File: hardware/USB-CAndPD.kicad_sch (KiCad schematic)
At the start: 28 parts, among them J201 USB_C_Receptacle_USB2.0_16P, J202 USB_C_Receptacle_USB2.0_16P, U201 TPS25730D, U202 TPD2E2U06DCK

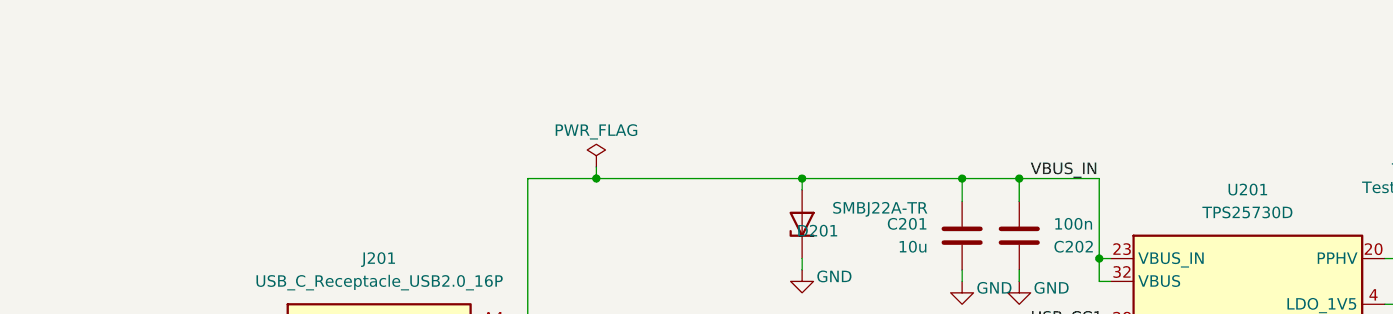
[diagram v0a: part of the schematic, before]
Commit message: Optimized BOM and added netties
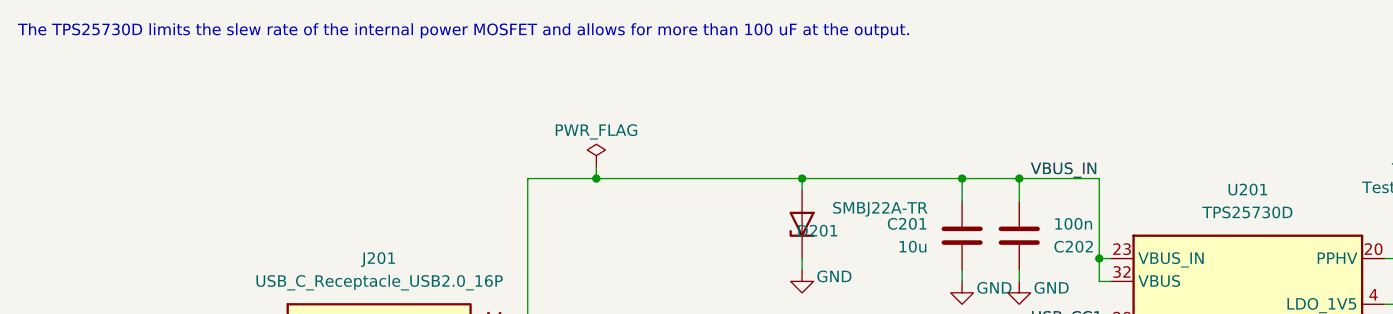
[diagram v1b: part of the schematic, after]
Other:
- note added: "The TPS25730D limits the slew rate of the internal power MOSFET and allows for more than 100 uF at the output."
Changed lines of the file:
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@@
+		)
+	)
+	(text "The TPS25730D limits the slew rate of the internal power MOSFET and allows for more than 100 uF at the output."
+		(exclude_from_sim no)
+		(at 15.748 16.002 0)
+		(effects
+			(font
+				(size 1.27 1.27)
+			)
+			(justify left top)
 		)
 	)

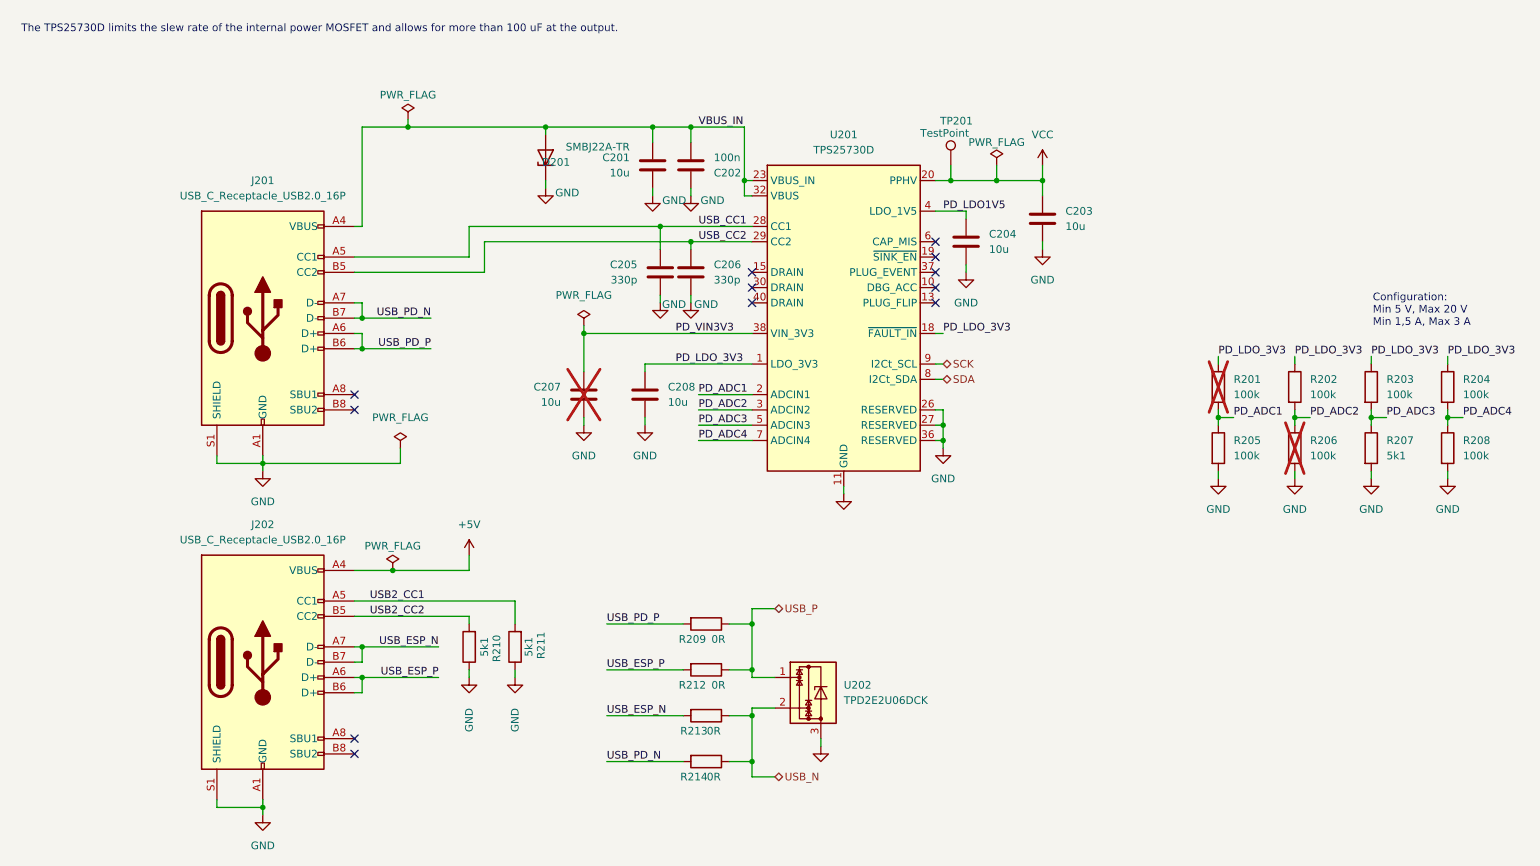
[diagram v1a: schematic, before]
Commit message: Spring terminal, finalising PD settings, checking buck 10 A
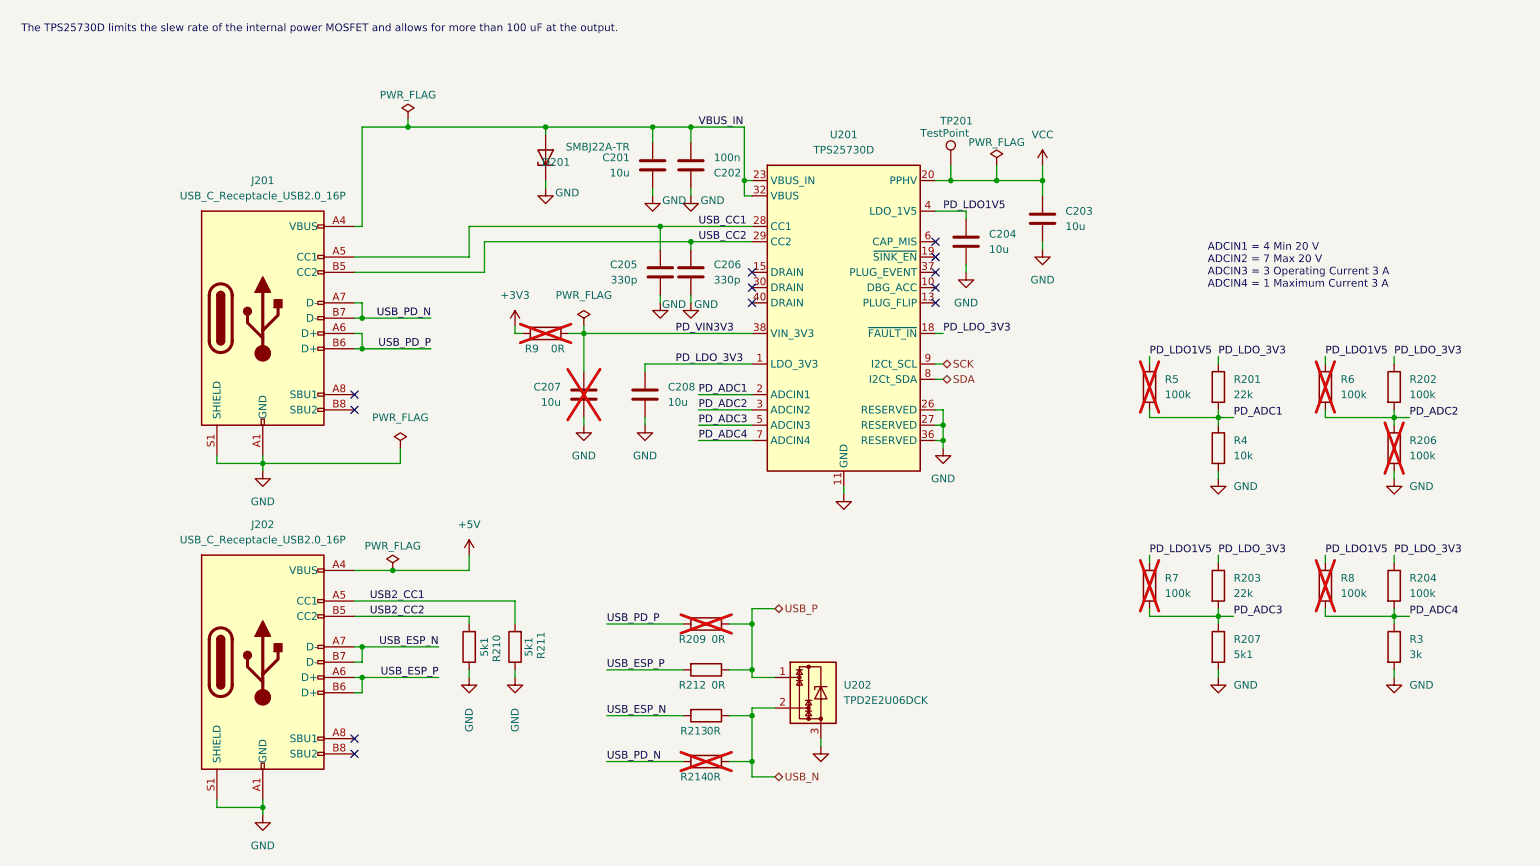
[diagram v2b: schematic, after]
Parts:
- removed R205, R208: 100k, Resistor_SMD:R_0603_1608Metric_Pad0.98x0.95mm_HandSolder, symbol Device:R
- added R3: 3k, Resistor_SMD:R_0603_1608Metric_Pad0.98x0.95mm_HandSolder, symbol Device:R
- added R4: 10k, Resistor_SMD:R_0603_1608Metric_Pad0.98x0.95mm_HandSolder, symbol Device:R
- added R5, R6, R7, R8: 100k, Resistor_SMD:R_0603_1608Metric_Pad0.98x0.95mm_HandSolder, symbol Device:R
- added R9: 0R, Resistor_SMD:R_0603_1608Metric_Pad0.98x0.95mm_HandSolder, symbol Device:R
- R201: value 100k -> 22k; now fitted
- R203: value 100k -> 22k
- R209, R214: now not fitted
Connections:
- net GND: now also R3.2, R4.2
- net PD_ADC1: now also R4.1, R5.2
- net PD_ADC2: now also R6.2
- net PD_ADC3: now also R7.2
- net PD_ADC4: now also R3.1, R8.2
- net PD_LDO1V5: now also R5.1, R6.1, R7.1, R8.1
- net PD_VIN3V3: now also R9.1
- new net +3V3: R9.2
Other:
- note added: "ADCIN1 = 4 Min 20 V ADCIN2 = 7 Max 20 V ADCIN3 = 3 Operating Current 3 A ADCIN4 = 1 Maximum Current 3 A"
- note removed: "Configuration: Min 5 V, Max 20 V Min 1,5 A, Max 3 A"
- moved on the sheet: R202, R203, R204, R206, R207

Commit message: Changed footprints to non hand solder option
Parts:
- C201, C203: footprint Capacitor_SMD:C_1210_3225Metric_Pad1.33x2.70mm_HandSolder -> Capacitor_SMD:C_1210_3225Metric
- C202, C204, C205, C206, C207, C208: footprint Capacitor_SMD:C_0603_1608Metric_Pad1.08x0.95mm_HandSolder -> Capacitor_SMD:C_0603_1608Metric
- R201, R202, R203, R204, R206, R207, R209, R210, R211, R212, R213, R214, R3, R4, R5, R6, R7, R8, R9: footprint Resistor_SMD:R_0603_1608Metric_Pad0.98x0.95mm_HandSolder -> Resistor_SMD:R_0603_1608Metric
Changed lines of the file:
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@@
 			)
 		)
-		(property "Footprint" "Resistor_SMD:R_0603_1608Metric_Pad0.98x0.95mm_HandSolder"
+		(property "Footprint" "Resistor_SMD:R_0603_1608Metric"
 			(at 212.852 76.2 90)
 			(effects
@@
 			)
 		)
-		(property "Footprint" "Capacitor_SMD:C_0603_1608Metric_Pad1.08x0.95mm_HandSolder"
+		(property "Footprint" "Capacitor_SMD:C_0603_1608Metric"
 			(at 171.7548 48.26 0)
 			(effects
@@
 			)
 		)
-		(property "Footprint" "Resistor_SMD:R_0603_1608Metric_Pad0.98x0.95mm_HandSolder"
+		(property "Footprint" "Resistor_SMD:R_0603_1608Metric"
 			(at 212.852 119.38 90)
 			(effects
@@
 			)
 		)
-		(property "Footprint" "Capacitor_SMD:C_1210_3225Metric_Pad1.33x2.70mm_HandSolder"
+		(property "Footprint" "Capacitor_SMD:C_1210_3225Metric"
 			(at 184.4548 44.45 0)
 			(effects
@@
 			)
 		)
-		(property "Footprint" "Resistor_SMD:R_0603_1608Metric_Pad0.98x0.95mm_HandSolder"
+		(property "Footprint" "Resistor_SMD:R_0603_1608Metric"
 			(at 212.852 86.36 90)
 			(effects
@@
 			)
 		)
-		(property "Footprint" "Capacitor_SMD:C_0603_1608Metric_Pad1.08x0.95mm_HandSolder"
+		(property "Footprint" "Capacitor_SMD:C_0603_1608Metric"
 			(at 127.9652 60.96 0)
 			(effects
@@
 			)
 		)
-		(property "Footprint" "Resistor_SMD:R_0603_1608Metric_Pad0.98x0.95mm_HandSolder"
+		(property "Footprint" "Resistor_SMD:R_0603_1608Metric"
 			(at 102.87 65.532 90)
 			(effects
@@
 			)
 		)
-		(property "Footprint" "Resistor_SMD:R_0603_1608Metric_Pad0.98x0.95mm_HandSolder"
+		(property "Footprint" "Resistor_SMD:R_0603_1608Metric"
 			(at 230.632 76.2 90)
 			(effects
@@
 			)
 		)
-		(property "Footprint" "Resistor_SMD:R_0603_1608Metric_Pad0.98x0.95mm_HandSolder"
+		(property "Footprint" "Resistor_SMD:R_0603_1608Metric"
 			(at 242.062 86.36 90)
 			(effects
@@
 			)
 		)
-		(property "Footprint" "Capacitor_SMD:C_0603_1608Metric_Pad1.08x0.95mm_HandSolder"
+		(property "Footprint" "Capacitor_SMD:C_0603_1608Metric"
 			(at 118.4148 73.66 0)
 			(effects
@@
 			)
 		)
-		(property "Footprint" "Resistor_SMD:R_0603_1608Metric_Pad0.98x0.95mm_HandSolder"
+		(property "Footprint" "Resistor_SMD:R_0603_1608Metric"
 			(at 129.54 129.032 90)
 			(effects
@@
 			)
 		)
-		(property "Footprint" "Resistor_SMD:R_0603_1608Metric_Pad0.98x0.95mm_HandSolder"
+		(property "Footprint" "Resistor_SMD:R_0603_1608Metric"
 			(at 242.062 109.22 90)
 			(effects
@@
 			)
 		)
-		(property "Footprint" "Capacitor_SMD:C_0603_1608Metric_Pad1.08x0.95mm_HandSolder"
+		(property "Footprint" "Capacitor_SMD:C_0603_1608Metric"
 			(at 126.0348 35.56 0)
 			(effects
@@
 			)
 		)
-		(property "Footprint" "Resistor_SMD:R_0603_1608Metric_Pad0.98x0.95mm_HandSolder"
+		(property "Footprint" "Resistor_SMD:R_0603_1608Metric"
 			(at 129.54 136.652 90)
 			(effects
@@
 			)
 		)
-		(property "Footprint" "Resistor_SMD:R_0603_1608Metric_Pad0.98x0.95mm_HandSolder"
+		(property "Footprint" "Resistor_SMD:R_0603_1608Metric"
 			(at 201.422 76.2 90)
 			(effects
@@
 			)
 		)
-		(property "Footprint" "Resistor_SMD:R_0603_1608Metric_Pad0.98x0.95mm_HandSolder"
+		(property "Footprint" "Resistor_SMD:R_0603_1608Metric"
 			(at 129.54 113.792 90)
 			(effects
@@
 			)
 		)
-		(property "Footprint" "Resistor_SMD:R_0603_1608Metric_Pad0.98x0.95mm_HandSolder"
+		(property "Footprint" "Resistor_SMD:R_0603_1608Metric"
 			(at 201.422 109.22 90)
 			(effects
@@
 			)
 		)
-		(property "Footprint" "Resistor_SMD:R_0603_1608Metric_Pad0.98x0.95mm_HandSolder"
+		(property "Footprint" "Resistor_SMD:R_0603_1608Metric"
 			(at 129.54 121.412 90)
 			(effects
@@
 			)
 		)
-		(property "Footprint" "Resistor_SMD:R_0603_1608Metric_Pad0.98x0.95mm_HandSolder"
+		(property "Footprint" "Resistor_SMD:R_0603_1608Metric"
 			(at 230.632 109.22 90)
 			(effects
@@
 			)
 		)
-		(property "Footprint" "Resistor_SMD:R_0603_1608Metric_Pad0.98x0.95mm_HandSolder"
+		(property "Footprint" "Resistor_SMD:R_0603_1608Metric"
 			(at 242.062 119.38 90)
 			(effects
@@
 			)
 		)
-		(property "Footprint" "Capacitor_SMD:C_0603_1608Metric_Pad1.08x0.95mm_HandSolder"
+		(property "Footprint" "Capacitor_SMD:C_0603_1608Metric"
 			(at 110.1852 73.66 0)
 			(effects
@@
 			)
 		)
-		(property "Footprint" "Resistor_SMD:R_0603_1608Metric_Pad0.98x0.95mm_HandSolder"
+		(property "Footprint" "Resistor_SMD:R_0603_1608Metric"
 			(at 99.568 119.38 90)
 			(effects
@@
 			)
 		)
-		(property "Footprint" "Capacitor_SMD:C_1210_3225Metric_Pad1.33x2.70mm_HandSolder"
+		(property "Footprint" "Capacitor_SMD:C_1210_3225Metric"
 			(at 121.6152 35.56 0)
 			(effects
@@
 			)
 		)
-		(property "Footprint" "Resistor_SMD:R_0603_1608Metric_Pad0.98x0.95mm_HandSolder"
+		(property "Footprint" "Resistor_SMD:R_0603_1608Metric"
 			(at 91.948 119.38 90)
 			(effects
@@
 			)
 		)
-		(property "Footprint" "Resistor_SMD:R_0603_1608Metric_Pad0.98x0.95mm_HandSolder"
+		(property "Footprint" "Resistor_SMD:R_0603_1608Metric"
 			(at 242.062 76.2 90)
 			(effects
@@
 			)
 		)
-		(property "Footprint" "Capacitor_SMD:C_0603_1608Metric_Pad1.08x0.95mm_HandSolder"
+		(property "Footprint" "Capacitor_SMD:C_0603_1608Metric"
 			(at 122.8852 60.96 0)
 			(effects
@@
 			)
 		)
-		(property "Footprint" "Resistor_SMD:R_0603_1608Metric_Pad0.98x0.95mm_HandSolder"
+		(property "Footprint" "Resistor_SMD:R_0603_1608Metric"
 			(at 212.852 109.22 90)
 			(effects
